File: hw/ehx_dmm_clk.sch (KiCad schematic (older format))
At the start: 43 parts

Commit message: Schematic annotated
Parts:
- gave numbers to parts that had none: 37

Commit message: Footprint assignment complete
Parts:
- C1, C4: value 25uF -> 33uF; footprint (none) -> Capacitor_THT:CP_Radial_D12.5mm_P5.00mm
- C2, C3, C6, C8: footprint (none) -> Capacitor_THT:C_Rect_L7.0mm_W2.5mm_P5.00mm
- C5, C7, C9: footprint (none) -> Capacitor_THT:C_Rect_L10.0mm_W3.0mm_P7.50mm_FKS3_FKP3
- D2: footprint (none) -> LED_THT:LED_D3.0mm
- J2, J3: footprint (none) -> Connector_PinHeader_2.54mm:PinHeader_1x02_P2.54mm_Vertical
- J4, RV1, RV2: footprint (none) -> Connector_PinHeader_2.54mm:PinHeader_1x03_P2.54mm_Vertical
- Q1, Q2: footprint Package_TO_SOT_THT:TO-92_Inline -> Package_TO_SOT_THT:TO-92_HandSolder
- R1, R10, R11, R12, R13, R14, R2, R3, R4, R5, R6, R7, R8, R9: footprint (none) -> Resistor_THT:R_Axial_DIN0207_L6.3mm_D2.5mm_P7.62mm_Horizontal
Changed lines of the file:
@@
 F 0 "R9" V 6245 3650 50  0000 C CNN
 F 1 "1K" V 6336 3650 50  0000 C CNN
-F 2 "" V 6490 3640 50  0001 C CNN
+F 2 "Resistor_THT:R_Axial_DIN0207_L6.3mm_D2.5mm_P7.62mm_Horizontal" V 6490 3640 50  0001 C CNN
 F 3 "" H 6450 3650 50  0001 C CNN
 	1    6450 3650
@@
 F 0 "Q1" H 7091 3604 50  0000 L CNN
 F 1 "2N5401" H 7091 3695 50  0000 L CNN
-F 2 "Package_TO_SOT_THT:TO-92_Inline" H 7100 3575 50  0001 L CIN
+F 2 "Package_TO_SOT_THT:TO-92_HandSolder" H 7100 3575 50  0001 L CIN
 F 3 "" H 6900 3650 50  0001 L CNN
 	1    6900 3650
@@
 F 0 "R11" H 7068 4346 50  0000 L CNN
 F 1 "4.7k" H 7068 4255 50  0000 L CNN
-F 2 "" V 7040 4290 50  0001 C CNN
+F 2 "Resistor_THT:R_Axial_DIN0207_L6.3mm_D2.5mm_P7.62mm_Horizontal" V 7040 4290 50  0001 C CNN
 F 3 "" H 7000 4300 50  0001 C CNN
 	1    7000 4300
@@
 P 1000 6600
 F 0 "C1" H 1115 6646 50  0000 L CNN
-F 1 "25uF" H 1115 6555 50  0000 L CNN
-F 2 "" H 1000 6600 50  0001 C CNN
+F 1 "33uF" H 1115 6555 50  0000 L CNN
+F 2 "Capacitor_THT:CP_Radial_D12.5mm_P5.00mm" H 1000 6600 50  0001 C CNN
 F 3 "" H 1000 6600 50  0001 C CNN
 	1    1000 6600
@@
 P 2500 6600
 F 0 "C4" H 2615 6646 50  0000 L CNN
-F 1 "25uF" H 2615 6555 50  0000 L CNN
-F 2 "" H 2500 6600 50  0001 C CNN
+F 1 "33uF" H 2615 6555 50  0000 L CNN
+F 2 "Capacitor_THT:CP_Radial_D12.5mm_P5.00mm" H 2500 6600 50  0001 C CNN
 F 3 "" H 2500 6600 50  0001 C CNN
 	1    2500 6600
@@
 F 0 "C5" H 3065 6646 50  0000 L CNN
 F 1 "100nF" H 3065 6555 50  0000 L CNN
-F 2 "" H 2988 6450 50  0001 C CNN
+F 2 "Capacitor_THT:C_Rect_L10.0mm_W3.0mm_P7.50mm_FKS3_FKP3" H 2988 6450 50  0001 C CNN
 F 3 "" H 2950 6600 50  0001 C CNN
 	1    2950 6600
@@
 F 0 "R10" V 6295 5300 50  0000 C CNN
 F 1 "1K" V 6386 5300 50  0000 C CNN
-F 2 "" V 6540 5290 50  0001 C CNN
+F 2 "Resistor_THT:R_Axial_DIN0207_L6.3mm_D2.5mm_P7.62mm_Horizontal" V 6540 5290 50  0001 C CNN
 F 3 "" H 6500 5300 50  0001 C CNN
 	1    6500 5300
@@
 F 0 "Q2" H 7091 5254 50  0000 L CNN
 F 1 "2N5401" H 7091 5345 50  0000 L CNN
-F 2 "Package_TO_SOT_THT:TO-92_Inline" H 7100 5225 50  0001 L CIN
+F 2 "Package_TO_SOT_THT:TO-92_HandSolder" H 7100 5225 50  0001 L CIN
 F 3 "" H 6900 5300 50  0001 L CNN
 	1    6900 5300
@@
 F 0 "R12" H 7068 5996 50  0000 L CNN
 F 1 "4.7k" H 7068 5905 50  0000 L CNN
-F 2 "" V 7040 5940 50  0001 C CNN
+F 2 "Resistor_THT:R_Axial_DIN0207_L6.3mm_D2.5mm_P7.62mm_Horizontal" V 7040 5940 50  0001 C CNN
 F 3 "" H 7000 5950 50  0001 C CNN
 	1    7000 5950
@@
 F 0 "C9" H 10015 4996 50  0000 L CNN
 F 1 "100nF" H 10015 4905 50  0000 L CNN
-F 2 "" H 9938 4800 50  0001 C CNN
+F 2 "Capacitor_THT:C_Rect_L10.0mm_W3.0mm_P7.50mm_FKS3_FKP3" H 9938 4800 50  0001 C CNN
 F 3 "" H 9900 4950 50  0001 C CNN
 	1    9900 4950
@@
 F 0 "J2" H 1950 3050 50  0000 L CNN
 F 1 "Conn_01x02" H 1950 2950 50  0000 L CNN
-F 2 "" H 2000 3250 50  0001 C CNN
+F 2 "Connector_PinHeader_2.54mm:PinHeader_1x02_P2.54mm_Vertical" H 2000 3250 50  0001 C CNN
 F 3 "" H 2000 3250 50  0001 C CNN
 	1    2000 3250
@@
 F 0 "R1" H 1868 2996 50  0000 L CNN
 F 1 "10k" H 1868 2905 50  0000 L CNN
-F 2 "" V 1840 2940 50  0001 C CNN
+F 2 "Resistor_THT:R_Axial_DIN0207_L6.3mm_D2.5mm_P7.62mm_Horizontal" V 1840 2940 50  0001 C CNN
 F 3 "" H 1800 2950 50  0001 C CNN
 	1    1800 2950
@@
 F 0 "C2" H 1515 2996 50  0000 L CNN
 F 1 "1nF" H 1515 2905 50  0000 L CNN
-F 2 "" H 1438 2800 50  0001 C CNN
+F 2 "Capacitor_THT:C_Rect_L7.0mm_W2.5mm_P5.00mm" H 1438 2800 50  0001 C CNN
 F 3 "" H 1400 2950 50  0001 C CNN
 	1    1400 2950
@@
 F 0 "R7" H 4868 2996 50  0000 L CNN
 F 1 "10R" H 4868 2905 50  0000 L CNN
-F 2 "" V 4840 2940 50  0001 C CNN
+F 2 "Resistor_THT:R_Axial_DIN0207_L6.3mm_D2.5mm_P7.62mm_Horizontal" V 4840 2940 50  0001 C CNN
 F 3 "" H 4800 2950 50  0001 C CNN
 	1    4800 2950
@@
 F 0 "R8" H 4600 3700 50  0000 L CNN
 F 1 "10R" H 4550 3600 50  0000 L CNN
-F 2 "" V 4840 3640 50  0001 C CNN
+F 2 "Resistor_THT:R_Axial_DIN0207_L6.3mm_D2.5mm_P7.62mm_Horizontal" V 4840 3640 50  0001 C CNN
 F 3 "" H 4800 3650 50  0001 C CNN
 	1    4800 3650
@@
 F 0 "R14" H 9568 1096 50  0000 L CNN
 F 1 "47k" H 9568 1005 50  0000 L CNN
-F 2 "" V 9540 1040 50  0001 C CNN
+F 2 "Resistor_THT:R_Axial_DIN0207_L6.3mm_D2.5mm_P7.62mm_Horizontal" V 9540 1040 50  0001 C CNN
 F 3 "" H 9500 1050 50  0001 C CNN
 	1    9500 1050
@@
 F 0 "RV2" H 4732 3346 50  0000 R CNN
 F 1 "R_POT_US" H 4732 3255 50  0000 R CNN
-F 2 "" H 4800 3300 50  0001 C CNN
+F 2 "Connector_PinHeader_2.54mm:PinHeader_1x03_P2.54mm_Vertical" H 4800 3300 50  0001 C CNN
 F 3 "" H 4800 3300 50  0001 C CNN
 	1    4800 3300
@@
 F 0 "R3" H 3518 2996 50  0000 L CNN
 F 1 "10R" H 3518 2905 50  0000 L CNN
-F 2 "" V 3490 2940 50  0001 C CNN
+F 2 "Resistor_THT:R_Axial_DIN0207_L6.3mm_D2.5mm_P7.62mm_Horizontal" V 3490 2940 50  0001 C CNN
 F 3 "" H 3450 2950 50  0001 C CNN
 	1    3450 2950
@@
 F 0 "R4" H 3250 3700 50  0000 L CNN
 F 1 "10R" H 3200 3600 50  0000 L CNN
-F 2 "" V 3490 3640 50  0001 C CNN
+F 2 "Resistor_THT:R_Axial_DIN0207_L6.3mm_D2.5mm_P7.62mm_Horizontal" V 3490 3640 50  0001 C CNN
 F 3 "" H 3450 3650 50  0001 C CNN
 	1    3450 3650
@@
 F 0 "RV1" H 3382 3346 50  0000 R CNN
 F 1 "R_POT_US" H 3382 3255 50  0000 R CNN
-F 2 "" H 3450 3300 50  0001 C CNN
+F 2 "Connector_PinHeader_2.54mm:PinHeader_1x03_P2.54mm_Vertical" H 3450 3300 50  0001 C CNN
 F 3 "" H 3450 3300 50  0001 C CNN
 	1    3450 3300
@@
 F 0 "D2" V 7838 1282 50  0000 R CNN
 F 1 "LED" V 7747 1282 50  0000 R CNN
-F 2 "" H 7800 1400 50  0001 C CNN
+F 2 "LED_THT:LED_D3.0mm" H 7800 1400 50  0001 C CNN
 F 3 "" H 7800 1400 50  0001 C CNN
 	1    7800 1400
@@
 F 0 "R13" H 7868 1796 50  0000 L CNN
 F 1 "4.7k" H 7868 1705 50  0000 L CNN
-F 2 "" V 7840 1740 50  0001 C CNN
+F 2 "Resistor_THT:R_Axial_DIN0207_L6.3mm_D2.5mm_P7.62mm_Horizontal" V 7840 1740 50  0001 C CNN
 F 3 "" H 7800 1750 50  0001 C CNN
 	1    7800 1750
@@
 F 0 "C7" H 3965 1096 50  0000 L CNN
 F 1 "100nF" H 3965 1005 50  0000 L CNN
-F 2 "" H 3888 900 50  0001 C CNN
+F 2 "Capacitor_THT:C_Rect_L10.0mm_W3.0mm_P7.50mm_FKS3_FKP3" H 3888 900 50  0001 C CNN
 F 3 "" H 3850 1050 50  0001 C CNN
 	1    3850 1050
@@
 F 0 "J3" H 1950 4800 50  0000 L CNN
 F 1 "Conn_01x02" H 1950 4700 50  0000 L CNN
-F 2 "" H 2000 5000 50  0001 C CNN
+F 2 "Connector_PinHeader_2.54mm:PinHeader_1x02_P2.54mm_Vertical" H 2000 5000 50  0001 C CNN
 F 3 "" H 2000 5000 50  0001 C CNN
 	1    2000 5000
@@
 F 0 "R2" H 1868 4746 50  0000 L CNN
 F 1 "10k" H 1868 4655 50  0000 L CNN
-F 2 "" V 1840 4690 50  0001 C CNN
+F 2 "Resistor_THT:R_Axial_DIN0207_L6.3mm_D2.5mm_P7.62mm_Horizontal" V 1840 4690 50  0001 C CNN
 F 3 "" H 1800 4700 50  0001 C CNN
 	1    1800 4700
@@
 F 0 "C3" H 1515 4746 50  0000 L CNN
 F 1 "1nF" H 1515 4655 50  0000 L CNN
-F 2 "" H 1438 4550 50  0001 C CNN
+F 2 "Capacitor_THT:C_Rect_L7.0mm_W2.5mm_P5.00mm" H 1438 4550 50  0001 C CNN
 F 3 "" H 1400 4700 50  0001 C CNN
 	1    1400 4700
@@
 F 0 "R5" H 3618 4746 50  0000 L CNN
 F 1 "10k" H 3618 4655 50  0000 L CNN
-F 2 "" V 3590 4690 50  0001 C CNN
+F 2 "Resistor_THT:R_Axial_DIN0207_L6.3mm_D2.5mm_P7.62mm_Horizontal" V 3590 4690 50  0001 C CNN
 F 3 "" H 3550 4700 50  0001 C CNN
 	1    3550 4700
@@
 F 0 "C6" H 3265 4746 50  0000 L CNN
 F 1 "1nF" H 3265 4655 50  0000 L CNN
-F 2 "" H 3188 4550 50  0001 C CNN
+F 2 "Capacitor_THT:C_Rect_L7.0mm_W2.5mm_P5.00mm" H 3188 4550 50  0001 C CNN
 F 3 "" H 3150 4700 50  0001 C CNN
 	1    3150 4700
@@
 F 0 "J4" H 4830 5042 50  0000 L CNN
 F 1 "Conn_01x03" H 4830 4951 50  0000 L CNN
-F 2 "" H 4750 5000 50  0001 C CNN
+F 2 "Connector_PinHeader_2.54mm:PinHeader_1x03_P2.54mm_Vertical" H 4750 5000 50  0001 C CNN
 F 3 "~" H 4750 5000 50  0001 C CNN
 	1    4750 5000
@@
 F 0 "R6" H 4368 5346 50  0000 L CNN
 F 1 "10k" H 4368 5255 50  0000 L CNN
-F 2 "" V 4340 5290 50  0001 C CNN
+F 2 "Resistor_THT:R_Axial_DIN0207_L6.3mm_D2.5mm_P7.62mm_Horizontal" V 4340 5290 50  0001 C CNN
 F 3 "" H 4300 5300 50  0001 C CNN
 	1    4300 5300
@@
 F 0 "C8" H 4015 5346 50  0000 L CNN
 F 1 "1nF" H 4015 5255 50  0000 L CNN
-F 2 "" H 3938 5150 50  0001 C CNN
+F 2 "Capacitor_THT:C_Rect_L7.0mm_W2.5mm_P5.00mm" H 3938 5150 50  0001 C CNN
 F 3 "" H 3900 5300 50  0001 C CNN
 	1    3900 5300

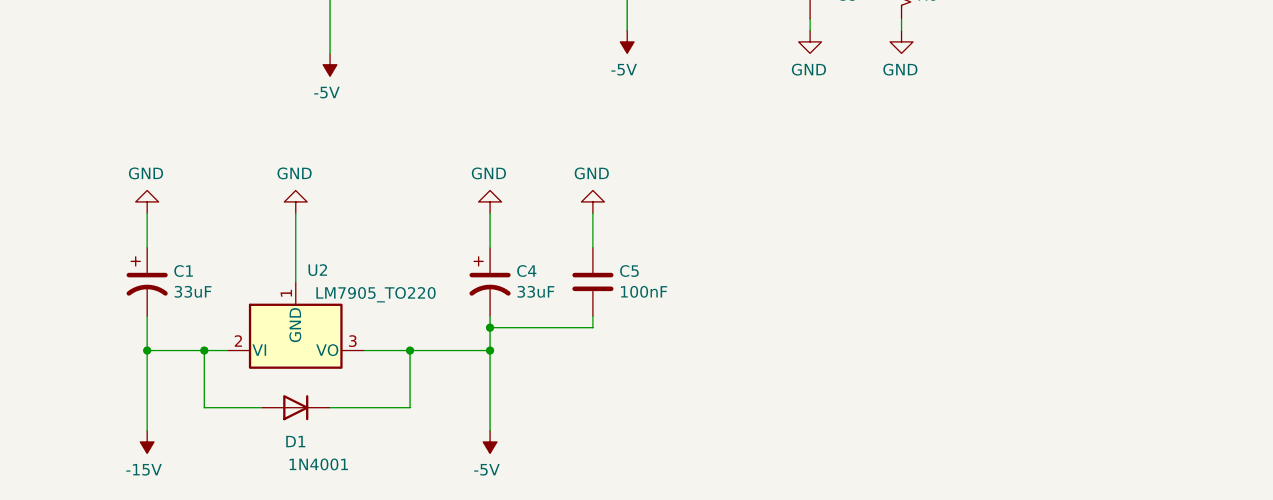
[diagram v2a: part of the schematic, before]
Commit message: Added connections for power input and clock output
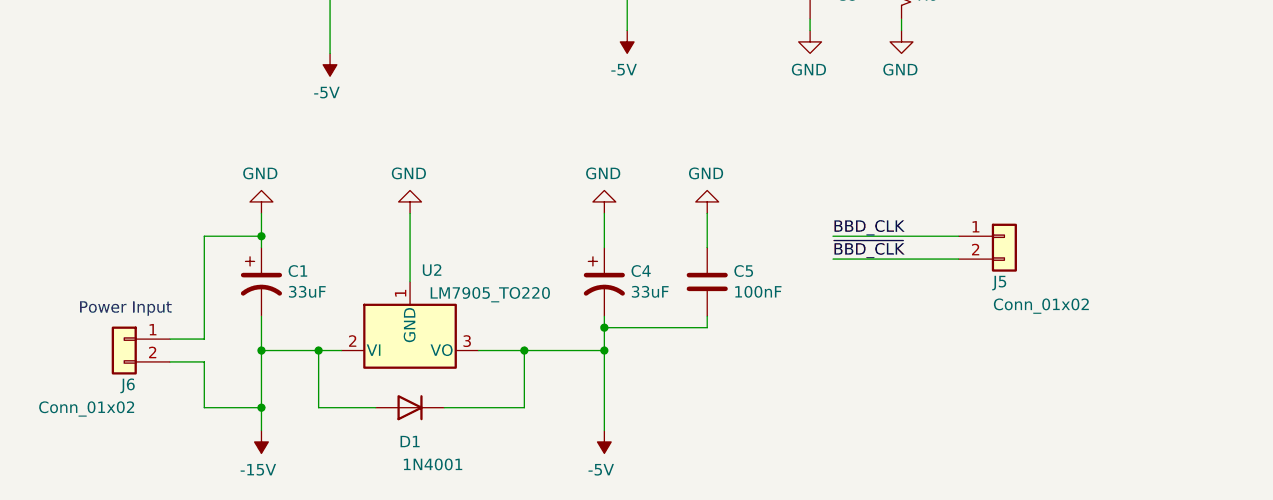
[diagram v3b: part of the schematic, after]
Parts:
- added J5, J6: Conn_01x02, Connector_PinHeader_2.54mm:PinHeader_1x02_P2.54mm_Vertical, symbol Connector_Generic:Conn_01x02
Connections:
- wire segments 129 -> 139
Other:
- note added: "Power Input"
- moved on the sheet: C1, C4, C5, D1, U2
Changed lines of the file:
@@
 L Regulator_Linear:LM7905_TO220 U2
 U 1 1 5F3B829C
-P 1650 6900
-F 0 "U2" H 1700 7250 50  0000 L CNN
-F 1 "LM7905_TO220" H 2000 7150 50  0000 C CNN
-F 2 "Package_TO_SOT_THT:TO-220-3_Vertical" H 1650 6700 50  0001 C CIN
-F 3 "" H 1650 6900 50  0001 C CNN
-	1    1650 6900
+P 2150 6900
+F 0 "U2" H 2200 7250 50  0000 L CNN
+F 1 "LM7905_TO220" H 2500 7150 50  0000 C CNN
+F 2 "Package_TO_SOT_THT:TO-220-3_Vertical" H 2150 6700 50  0001 C CIN
+F 3 "" H 2150 6900 50  0001 C CNN
+	1    2150 6900
 	1    0    0    -1
 $EndComp
@@
 L power:-15V #PWR0105
 U 1 1 5F3B8473
-P 1000 7250
-F 0 "#PWR0105" H 1000 7350 50  0001 C CNN
-F 1 "-15V" H 1015 7423 50  0000 C CNN
-F 2 "" H 1000 7250 50  0001 C CNN
-F 3 "" H 1000 7250 50  0001 C CNN
-	1    1000 7250
+P 1500 7250
+F 0 "#PWR0105" H 1500 7350 50  0001 C CNN
+F 1 "-15V" H 1515 7423 50  0000 C CNN
+F 2 "" H 1500 7250 50  0001 C CNN
+F 3 "" H 1500 7250 50  0001 C CNN
+	1    1500 7250
 	-1   0    0    1
 $EndComp
@@
 L power:-5V #PWR0106
 U 1 1 5F3B8507
-P 2500 7250
-F 0 "#PWR0106" H 2500 7350 50  0001 C CNN
-F 1 "-5V" H 2515 7423 50  0000 C CNN
-F 2 "" H 2500 7250 50  0001 C CNN
-F 3 "" H 2500 7250 50  0001 C CNN
-	1    2500 7250
+P 3000 7250
+F 0 "#PWR0106" H 3000 7350 50  0001 C CNN
+F 1 "-5V" H 3015 7423 50  0000 C CNN
+F 2 "" H 3000 7250 50  0001 C CNN
+F 3 "" H 3000 7250 50  0001 C CNN
+	1    3000 7250
 	-1   0    0    1
 $EndComp
@@
 L Device:CP1 C1
 U 1 1 5F3B8668
-P 1000 6600
-F 0 "C1" H 1115 6646 50  0000 L CNN
-F 1 "33uF" H 1115 6555 50  0000 L CNN
-F 2 "Capacitor_THT:CP_Radial_D12.5mm_P5.00mm" H 1000 6600 50  0001 C CNN
-F 3 "" H 1000 6600 50  0001 C CNN
-	1    1000 6600
+P 1500 6600
+F 0 "C1" H 1615 6646 50  0000 L CNN
+F 1 "33uF" H 1615 6555 50  0000 L CNN
+F 2 "Capacitor_THT:CP_Radial_D12.5mm_P5.00mm" H 1500 6600 50  0001 C CNN
+F 3 "" H 1500 6600 50  0001 C CNN
+	1    1500 6600
 	1    0    0    -1
 $EndComp
@@
 L power:GND #PWR0107
 U 1 1 5F3B878A
-P 1650 6300
-F 0 "#PWR0107" H 1650 6050 50  0001 C CNN
-F 1 "GND" H 1655 6127 50  0000 C CNN
-F 2 "" H 1650 6300 50  0001 C CNN
-F 3 "" H 1650 6300 50  0001 C CNN
-	1    1650 6300
+P 2150 6300
+F 0 "#PWR0107" H 2150 6050 50  0001 C CNN
+F 1 "GND" H 2155 6127 50  0000 C CNN
+F 2 "" H 2150 6300 50  0001 C CNN
+F 3 "" H 2150 6300 50  0001 C CNN
+	1    2150 6300
 	-1   0    0    1
 $EndComp
@@
 L Device:CP1 C4
 U 1 1 5F3B8889
-P 2500 6600
-F 0 "C4" H 2615 6646 50  0000 L CNN
-F 1 "33uF" H 2615 6555 50  0000 L CNN
-F 2 "Capacitor_THT:CP_Radial_D12.5mm_P5.00mm" H 2500 6600 50  0001 C CNN
-F 3 "" H 2500 6600 50  0001 C CNN
-	1    2500 6600
+P 3000 6600
+F 0 "C4" H 3115 6646 50  0000 L CNN
+F 1 "33uF" H 3115 6555 50  0000 L CNN
+F 2 "Capacitor_THT:CP_Radial_D12.5mm_P5.00mm" H 3000 6600 50  0001 C CNN
+F 3 "" H 3000 6600 50  0001 C CNN
+	1    3000 6600
 	1    0    0    -1
 $EndComp
@@
 L power:GND #PWR0108
 U 1 1 5F3B88F9
-P 1000 6300
-F 0 "#PWR0108" H 1000 6050 50  0001 C CNN
-F 1 "GND" H 1005 6127 50  0000 C CNN
-F 2 "" H 1000 6300 50  0001 C CNN
-F 3 "" H 1000 6300 50  0001 C CNN
-	1    1000 6300
+P 1500 6300
+F 0 "#PWR0108" H 1500 6050 50  0001 C CNN
+F 1 "GND" H 1505 6127 50  0000 C CNN
+F 2 "" H 1500 6300 50  0001 C CNN
+F 3 "" H 1500 6300 50  0001 C CNN
+	1    1500 6300
 	-1   0    0    1
 $EndComp
@@
 L power:GND #PWR0109
 U 1 1 5F3B8920
-P 2500 6300
-F 0 "#PWR0109" H 2500 6050 50  0001 C CNN
-F 1 "GND" H 2505 6127 50  0000 C CNN
-F 2 "" H 2500 6300 50  0001 C CNN
-F 3 "" H 2500 6300 50  0001 C CNN
-	1    2500 6300
-	-1   0    0    1
-$EndComp
-Wire Wire Line
-	2500 6300 2500 6450
-Wire Wire Line
-	1650 6300 1650 6600
-Wire Wire Line
-	1000 6300 1000 6450
-Wire Wire Line
-	1350 6900 1250 6900
-Wire Wire Line
-	1000 6900 1000 7250
-Wire Wire Line
-	1000 6750 1000 6900
-Connection ~ 1000 6900
+P 3000 6300
+F 0 "#PWR0109" H 3000 6050 50  0001 C CNN
+F 1 "GND" H 3005 6127 50  0000 C CNN
+F 2 "" H 3000 6300 50  0001 C CNN
+F 3 "" H 3000 6300 50  0001 C CNN
+	1    3000 6300
+	-1   0    0    1
+$EndComp
+Wire Wire Line
+	3000 6300 3000 6450
+Wire Wire Line
+	2150 6300 2150 6600
+Wire Wire Line
+	1500 6300 1500 6400
+Wire Wire Line
+	1850 6900 1750 6900
+Wire Wire Line
+	1500 6900 1500 7150
+Wire Wire Line
+	1500 6750 1500 6900
+Connection ~ 1500 6900
 $Comp
 L Diode:1N4001 D1
 U 1 1 5F3B86A4
-P 1650 7150
-F 0 "D1" H 1650 7300 50  0000 C CNN
-F 1 "1N4001" H 1550 7400 50  0000 C CNN
-F 2 "Diode_THT:D_DO-41_SOD81_P10.16mm_Horizontal" H 1650 6975 50  0001 C CNN
-F 3 "" H 1650 7150 50  0001 C CNN
-	1    1650 7150
-	-1   0    0    1
-$EndComp
-Wire Wire Line
-	1950 6900 2150 6900
-Wire Wire Line
-	1800 7150 2150 7150
-Wire Wire Line
-	2150 7150 2150 6900
-Wire Wire Line
-	1500 7150 1250 7150
-Wire Wire Line
-	1250 7150 1250 6900
-Connection ~ 1250 6900
-Wire Wire Line
-	1250 6900 1000 6900
+P 2150 7150
+F 0 "D1" H 2150 7300 50  0000 C CNN
+F 1 "1N4001" H 2050 7400 50  0000 C CNN
+F 2 "Diode_THT:D_DO-41_SOD81_P10.16mm_Horizontal" H 2150 6975 50  0001 C CNN
+F 3 "" H 2150 7150 50  0001 C CNN
+	1    2150 7150
+	-1   0    0    1
+$EndComp
+Wire Wire Line
+	2450 6900 2650 6900
+Wire Wire Line
+	2300 7150 2650 7150
+Wire Wire Line
+	2650 7150 2650 6900
+Wire Wire Line
+	2000 7150 1750 7150
+Wire Wire Line
+	1750 7150 1750 6900
+Connection ~ 1750 6900
+Wire Wire Line
+	1750 6900 1500 6900
 $Comp
 L Device:C C5
 U 1 1 5F3B9954
-P 2950 6600
-F 0 "C5" H 3065 6646 50  0000 L CNN
-F 1 "100nF" H 3065 6555 50  0000 L CNN
-F 2 "Capacitor_THT:C_Rect_L10.0mm_W3.0mm_P7.50mm_FKS3_FKP3" H 2988 6450 50  0001 C CNN
-F 3 "" H 2950 6600 50  0001 C CNN
-	1    2950 6600
+P 3450 6600
+F 0 "C5" H 3565 6646 50  0000 L CNN
+F 1 "100nF" H 3565 6555 50  0000 L CNN
+F 2 "Capacitor_THT:C_Rect_L10.0mm_W3.0mm_P7.50mm_FKS3_FKP3" H 3488 6450 50  0001 C CNN
+F 3 "" H 3450 6600 50  0001 C CNN
+	1    3450 6600
 	1    0    0    -1
 $EndComp
@@
 L power:GND #PWR0110
 U 1 1 5F3B9C74
-P 2950 6300
-F 0 "#PWR0110" H 2950 6050 50  0001 C CNN
-F 1 "GND" H 2955 6127 50  0000 C CNN
-F 2 "" H 2950 6300 50  0001 C CNN
-F 3 "" H 2950 6300 50  0001 C CNN
-	1    2950 6300
-	-1   0    0    1
-$EndComp
-Wire Wire Line
-	2950 6300 2950 6450
-Wire Wire Line
-	2500 6750 2500 6800
-Wire Wire Line
-	2150 6900 2500 6900
-Connection ~ 2150 6900
-Connection ~ 2500 6900
-Wire Wire Line
-	2500 6900 2500 7250
-Wire Wire Line
-	2500 6800 2950 6800
-Wire Wire Line
-	2950 6800 2950 6750
-Connection ~ 2500 6800
-Wire Wire Line
-	2500 6800 2500 6900
+P 3450 6300
+F 0 "#PWR0110" H 3450 6050 50  0001 C CNN
+F 1 "GND" H 3455 6127 50  0000 C CNN
+F 2 "" H 3450 6300 50  0001 C CNN
+F 3 "" H 3450 6300 50  0001 C CNN
+	1    3450 6300
+	-1   0    0    1
+$EndComp
+Wire Wire Line
+	3450 6300 3450 6450
+Wire Wire Line
+	3000 6750 3000 6800
+Wire Wire Line
+	2650 6900 3000 6900
+Connection ~ 2650 6900
+Connection ~ 3000 6900
+Wire Wire Line
+	3000 6900 3000 7250
+Wire Wire Line
+	3000 6800 3450 6800
+Wire Wire Line
+	3450 6800 3450 6750
+Connection ~ 3000 6800
+Wire Wire Line
+	3000 6800 3000 6900
 $Comp
 L Device:R_US R10
@@
 	4550 5100 4300 5100
 Connection ~ 4300 5100
+$Comp
+L Connector_Generic:Conn_01x02 J5
+U 1 1 5F43BAD2
+P 4750 6400
+F 0 "J5" H 4700 6200 50  0000 L CNN
+F 1 "Conn_01x02" H 4700 6100 50  0000 L CNN
+F 2 "Connector_PinHeader_2.54mm:PinHeader_1x02_P2.54mm_Vertical" H 4750 6400 50  0001 C CNN
+F 3 "" H 4750 6400 50  0001 C CNN
+	1    4750 6400
+	1    0    0    -1
+$EndComp
+Text Label 4000 6500 0    50   ~ 0
+~BBD_CLK
+Text Label 4000 6400 0    50   ~ 0
+BBD_CLK
+Wire Wire Line
+	4000 6400 4550 6400
+Wire Wire Line
+	4000 6500 4550 6500
+$Comp
+L Connector_Generic:Conn_01x02 J6
+U 1 1 5F44F71D
+P 900 6850
+F 0 "J6" H 850 6650 50  0000 L CNN
+F 1 "Conn_01x02" H 850 6550 50  0000 L CNN
+F 2 "Connector_PinHeader_2.54mm:PinHeader_1x02_P2.54mm_Vertical" H 900 6850 50  0001 C CNN
+F 3 "" H 900 6850 50  0001 C CNN
+	1    900  6850
+	-1   0    0    -1
+$EndComp
+Wire Wire Line
+	1100 6850 1250 6850
+Wire Wire Line
+	1250 6850 1250 6400
+Wire Wire Line
+	1250 6400 1500 6400
+Connection ~ 1500 6400
+Wire Wire Line
+	1500 6400 1500 6450
+Wire Wire Line
+	1100 6950 1250 6950
+Wire Wire Line
+	1250 6950 1250 7150
+Wire Wire Line
+	1250 7150 1500 7150
+Connection ~ 1500 7150
+Wire Wire Line
+	1500 7150 1500 7250
+Text Notes 700  6750 0    50   ~ 0
+Power Input
 $EndSCHEMATC

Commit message: Removed some unnecessary resistors
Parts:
- removed R3, R4, R7, R8: 10R, Resistor_THT:R_Axial_DIN0207_L6.3mm_D2.5mm_P7.62mm_Horizontal, symbol Device:R_US
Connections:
- wire segments 139 -> 135
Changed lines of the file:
@@
 CHORUS_AMOUNT
-$Comp
-L Device:R_US R7
-U 1 1 5F42B961
-P 4800 2950
-F 0 "R7" H 4868 2996 50  0000 L CNN
-F 1 "10R" H 4868 2905 50  0000 L CNN
-F 2 "Resistor_THT:R_Axial_DIN0207_L6.3mm_D2.5mm_P7.62mm_Horizontal" V 4840 2940 50  0001 C CNN
-F 3 "" H 4800 2950 50  0001 C CNN
-	1    4800 2950
-	1    0    0    -1
-$EndComp
 $Comp
 L power:GND #PWR0121
@@
 	-1   0    0    1
 $EndComp
-Wire Wire Line
-	4800 3150 4800 3100
-Wire Wire Line
-	4800 2800 4800 2750
-$Comp
-L Device:R_US R8
-U 1 1 5F42B975
-P 4800 3650
-F 0 "R8" H 4600 3700 50  0000 L CNN
-F 1 "10R" H 4550 3600 50  0000 L CNN
-F 2 "Resistor_THT:R_Axial_DIN0207_L6.3mm_D2.5mm_P7.62mm_Horizontal" V 4840 3640 50  0001 C CNN
-F 3 "" H 4800 3650 50  0001 C CNN
-	1    4800 3650
-	1    0    0    -1
-$EndComp
-Wire Wire Line
-	4800 3500 4800 3450
-Wire Wire Line
-	4800 3800 4800 3850
 Wire Wire Line
 	4650 3300 3950 3300
@@
 $EndComp
 $Comp
-L Device:R_US R3
-U 1 1 5F443F69
-P 3450 2950
-F 0 "R3" H 3518 2996 50  0000 L CNN
-F 1 "10R" H 3518 2905 50  0000 L CNN
-F 2 "Resistor_THT:R_Axial_DIN0207_L6.3mm_D2.5mm_P7.62mm_Horizontal" V 3490 2940 50  0001 C CNN
-F 3 "" H 3450 2950 50  0001 C CNN
-	1    3450 2950
-	1    0    0    -1
-$EndComp
-$Comp
 L power:GND #PWR06
 U 1 1 5F443F6F
@@
 	-1   0    0    1
 $EndComp
-Wire Wire Line
-	3450 3150 3450 3100
-Wire Wire Line
-	3450 2800 3450 2750
-$Comp
-L Device:R_US R4
-U 1 1 5F443F7D
-P 3450 3650
-F 0 "R4" H 3250 3700 50  0000 L CNN
-F 1 "10R" H 3200 3600 50  0000 L CNN
-F 2 "Resistor_THT:R_Axial_DIN0207_L6.3mm_D2.5mm_P7.62mm_Horizontal" V 3490 3640 50  0001 C CNN
-F 3 "" H 3450 3650 50  0001 C CNN
-	1    3450 3650
-	1    0    0    -1
-$EndComp
-Wire Wire Line
-	3450 3500 3450 3450
-Wire Wire Line
-	3450 3800 3450 3850
 $Comp
 L Device:R_POT_US RV1
@@
 Text Notes 700  6750 0    50   ~ 0
 Power Input
+Wire Wire Line
+	3450 2750 3450 3150
+Wire Wire Line
+	3450 3450 3450 3850
+Wire Wire Line
+	4800 2750 4800 3150
+Wire Wire Line
+	4800 3450 4800 3850
 $EndSCHEMATC
